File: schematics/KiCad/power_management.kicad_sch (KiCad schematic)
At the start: 47 parts, among them J3 USB_C, Q1 DMG6601LVT-7, Q2 DMG6601LVT-7, Q3 DMG9926UDM, SW4 K2-1102AQ-C4CW-01, U4 AP2112K-3.3, U6 BQ29700DSER, U7 MAX40200AUK, U8 BQ25618

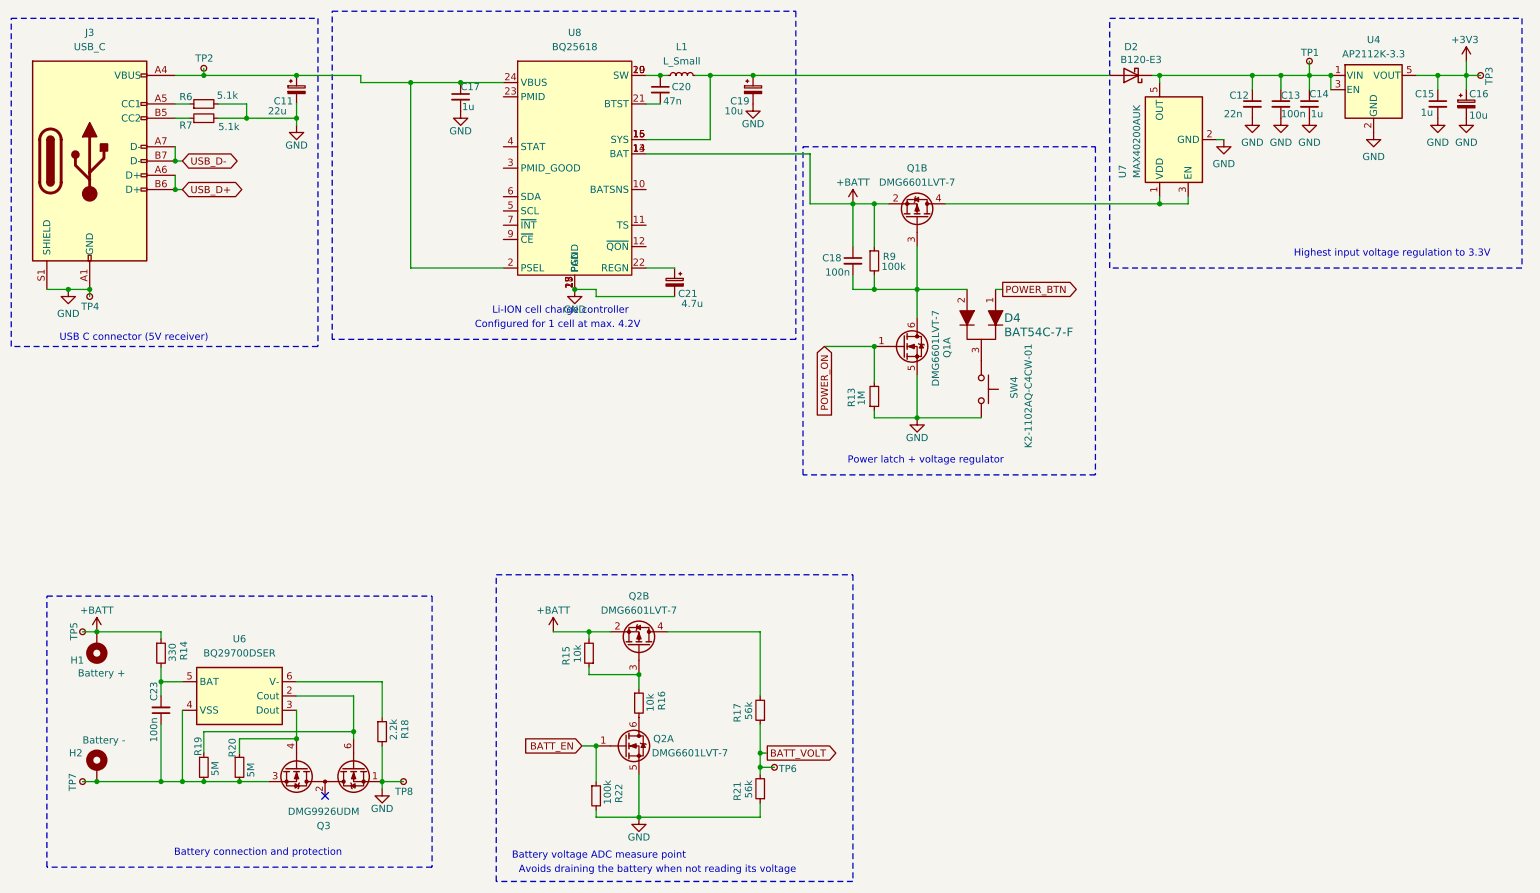
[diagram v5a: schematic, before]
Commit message: remove redundant battery protection IC
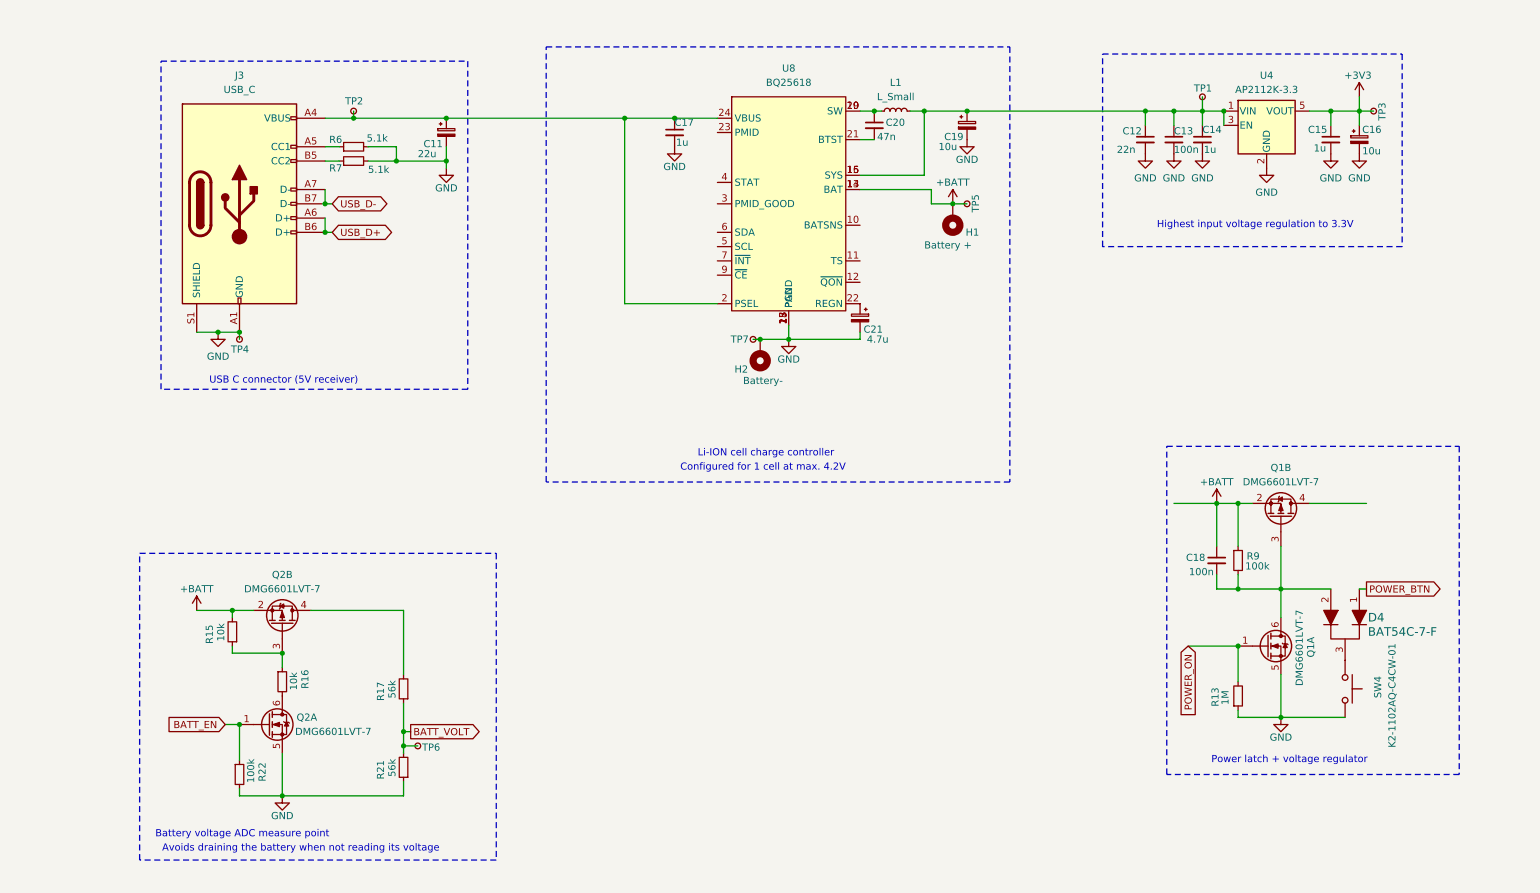
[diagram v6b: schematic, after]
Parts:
- removed C23: 100n, Capacitor_SMD:C_0603_1608Metric, symbol Device:C_Small
- removed D2: B120-E3, Diode_SMD:D_SMA, symbol Diode:B120-E3
- removed Q3: DMG9926UDM, Package_TO_SOT_SMD:SOT-23-6, symbol Transistor_FET:DMG9926UDM
- removed R14: 330, Resistor_SMD:R_0603_1608Metric, symbol Device:R_Small
- removed R18: 2.2k, Resistor_SMD:R_0603_1608Metric, symbol Device:R_Small
- removed R19, R20: 5M, Resistor_SMD:R_0603_1608Metric, symbol Device:R_Small
- removed TP8: GND, TestPoint:TestPoint_Pad_1.0x1.0mm, symbol Connector:TestPoint_Small
- removed U6: BQ29700DSER, Package_SON:WSON-6_1.5x1.5mm_P0.5mm, symbol leany-symbols:BQ29700DSER
- removed U7: MAX40200AUK, Package_TO_SOT_SMD:SOT-23-5, symbol Analog_Switch:MAX40200AUK
- H2: value Battery - -> Battery-
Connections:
- net GND: now also H2.MP, TP7.1
- net at C19.1, L1.2, U8.15 (SYS)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: now also C12.1, C13.1, C14.1, TP1.1, U4.1 (VIN), U4.3 (EN)
- no-connect marks 1 -> 0
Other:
- note removed: "Battery connection and protection"
- moved on the sheet: C11, C12, C13, C14, C15, C16, C17, C18, C19, C20, C21, D4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

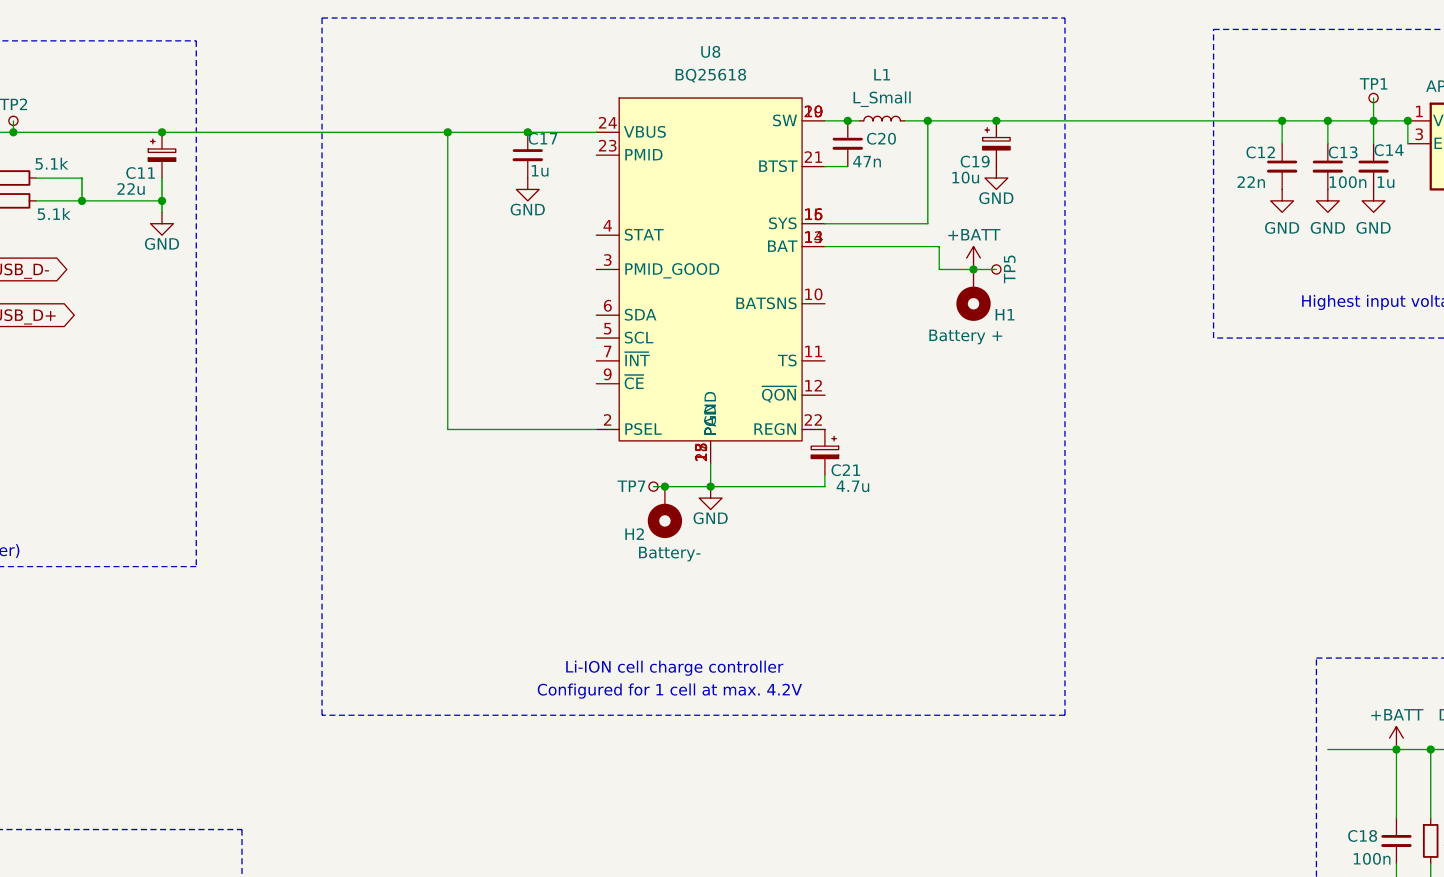
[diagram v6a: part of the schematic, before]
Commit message: assign charge manager pins
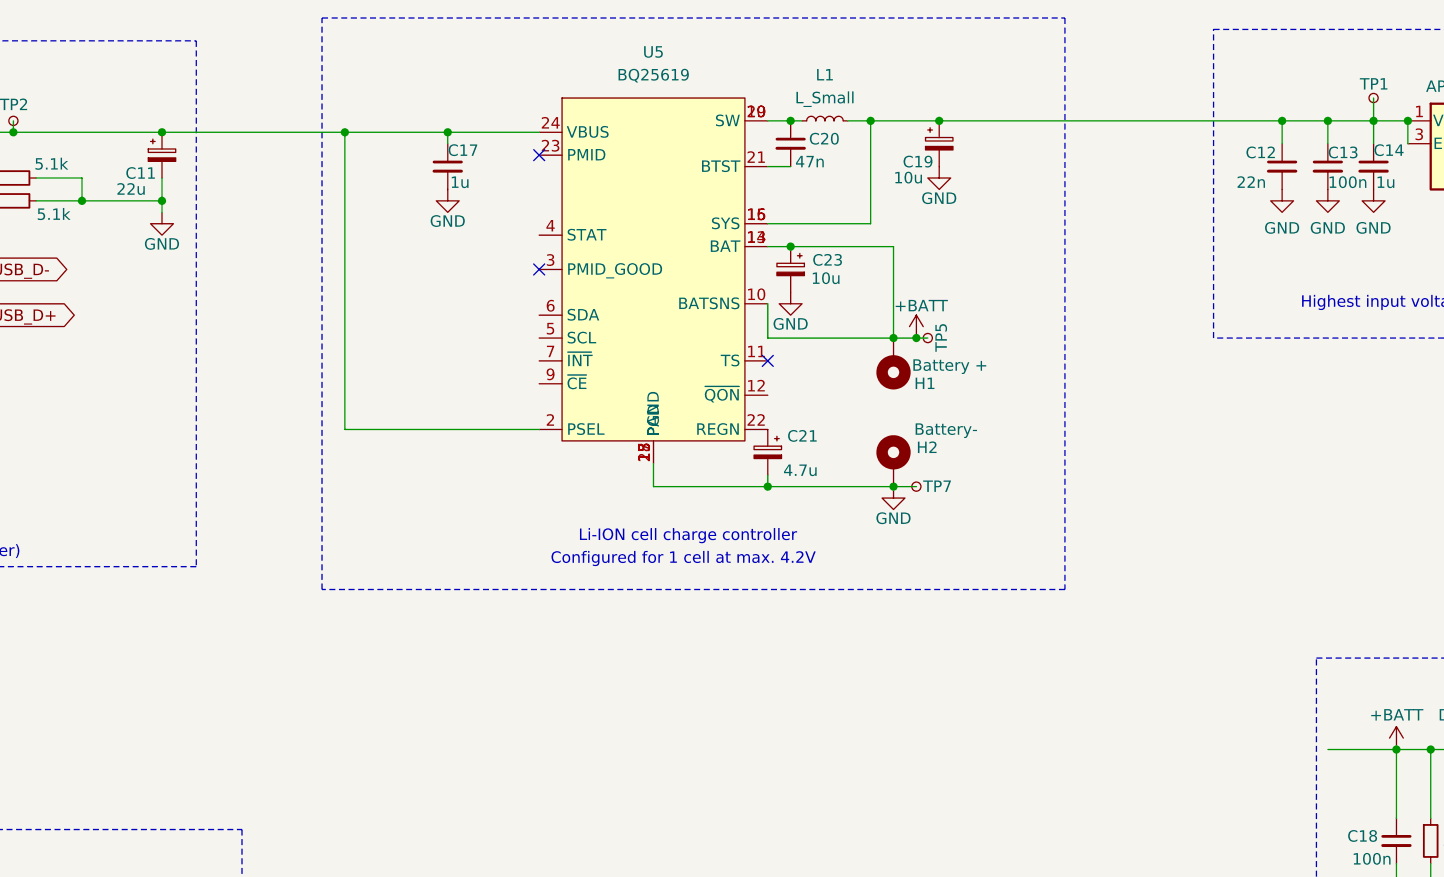
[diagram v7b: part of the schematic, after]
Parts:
- removed U8: BQ25618, Package_DFN_QFN:Texas_RGE0024H_VQFN-24-1EP_4x4mm_P0.5mm_EP2.7x2.7mm_ThermalVias, symbol leany-symbols:BQ25618
- added C23: 10u, Capacitor_Tantalum_SMD:CP_EIA-7343-31_Kemet-D, symbol Device:C_Polarized_Small
- added U5: BQ25619, Package_DFN_QFN:Texas_RGE0024H_VQFN-24-1EP_4x4mm_P0.5mm_EP2.7x2.7mm_ThermalVias, symbol leany-symbols:BQ25619
- C19: footprint Capacitor_SMD:C_0805_2012Metric -> Capacitor_Tantalum_SMD:CP_EIA-7343-31_Kemet-D
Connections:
- net +BATT: now also C23.1, U5.10 (BATSNS), U5.13 (BAT), U5.14 (BAT)
- net GND: now also C23.2, U5.17 (PGND), U5.18 (PGND), U5.25 (PAD)
- net at C11.1, C17.1, J3.A4 (VBUS)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: now also U5.1 (VAC), U5.2 (PSEL), U5.24 (VBUS)
- net at C20.1, L1.1: now also U5.19 (SW), U5.20 (SW)
- net at C12.1, C13.1, C14.1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: now also U5.15 (SYS), U5.16 (SYS)
- net at C21.1: now also U5.22 (REGN)
- net at C20.2: now also U5.21 (BTST)
- no-connect marks 0 -> 3
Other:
- moved on the sheet: C17, C19, C20, C21, H1, H2, L1, TP5, TP7

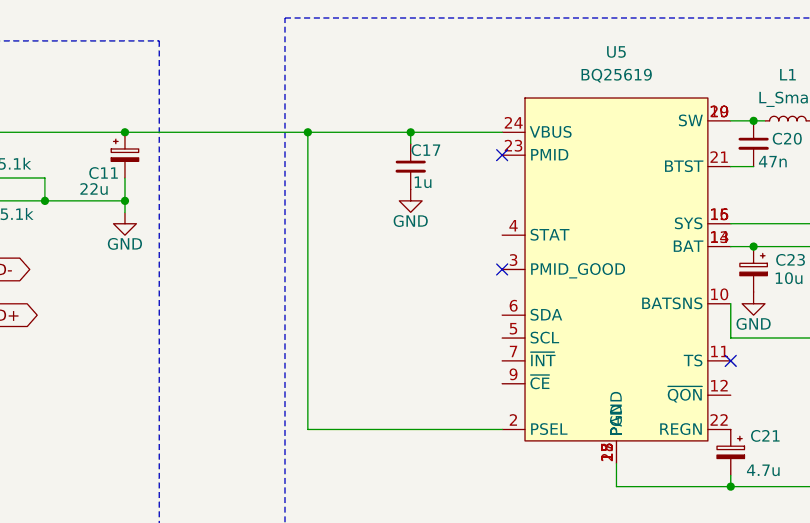
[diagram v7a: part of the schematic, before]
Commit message: enable I2C1 and connect it to charger
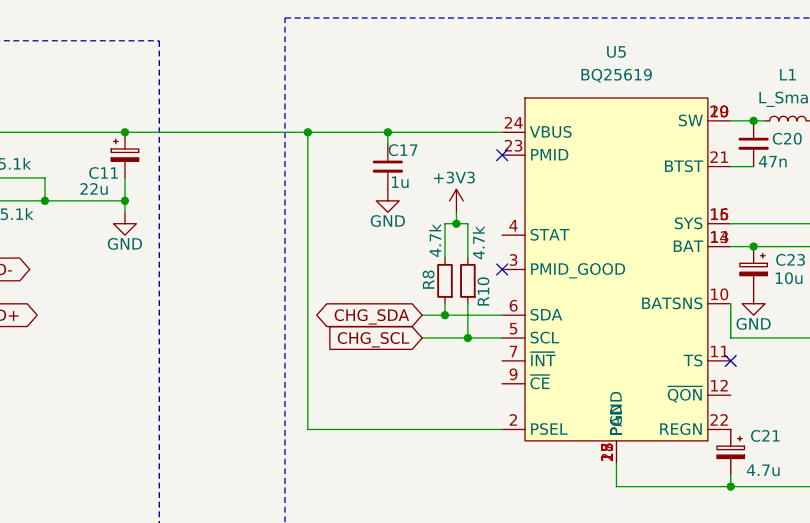
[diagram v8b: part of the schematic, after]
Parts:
- added R10, R8: 4.7k, Resistor_SMD:R_0603_1608Metric, symbol Device:R_Small
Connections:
- net +3V3: now also R10.2, R8.2
- net CHG_SCL: now reaches U5.5 (SCL)
- net CHG_SCL: now also R10.1
- net CHG_SDA: now reaches U5.6 (SDA)
- net CHG_SDA: now also R8.1
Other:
- moved on the sheet: C17
